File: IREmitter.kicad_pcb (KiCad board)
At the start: 2 copper layers, 36 parts, among them J1 JST Connector, J2 JST Connector, J3 Right Header, J4 Left Header, SW1 Switch, U1 MOSFET, U2 H-Bridge, U3 Voltage Regulator, U4 STM32F205RGTx

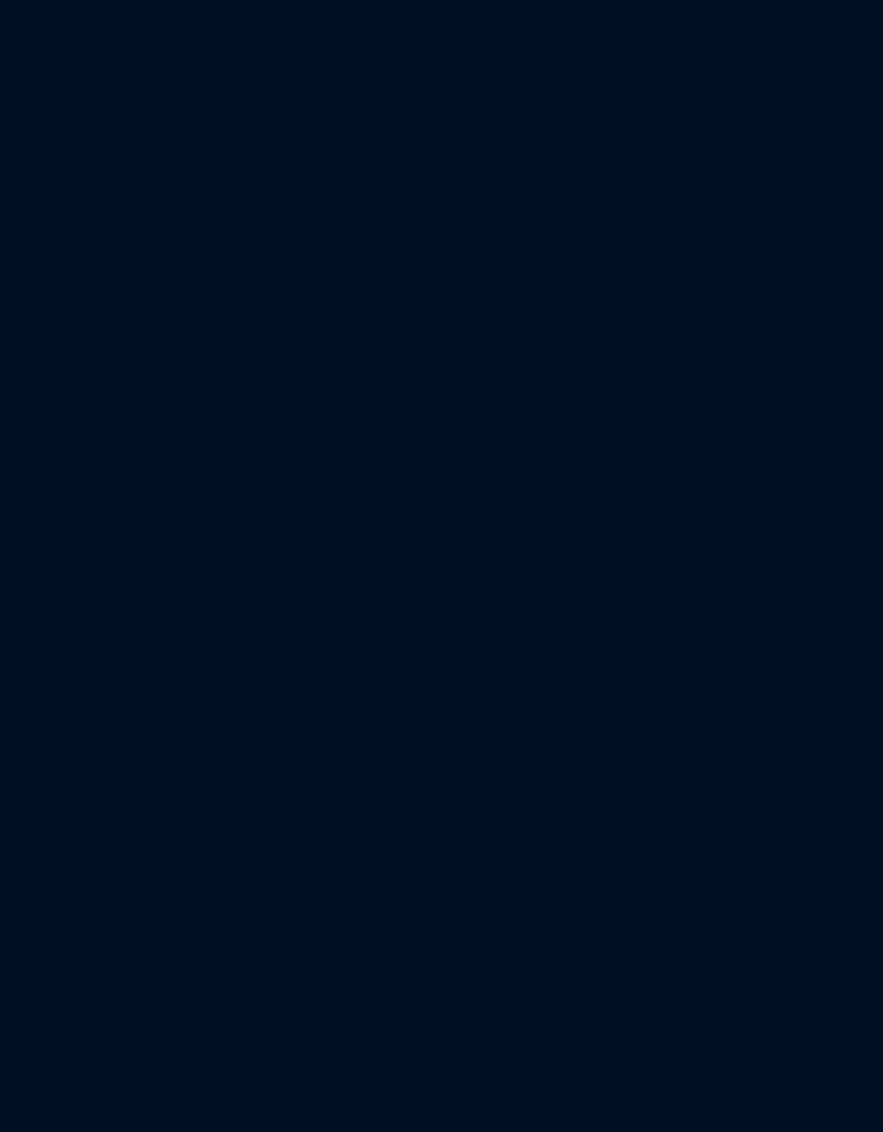
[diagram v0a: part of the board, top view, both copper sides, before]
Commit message: redid the 4 emitters receivers, fixed orientation of LEDS and going to continue adding footprints and replace the 60ohm resistors with 300ohm ones
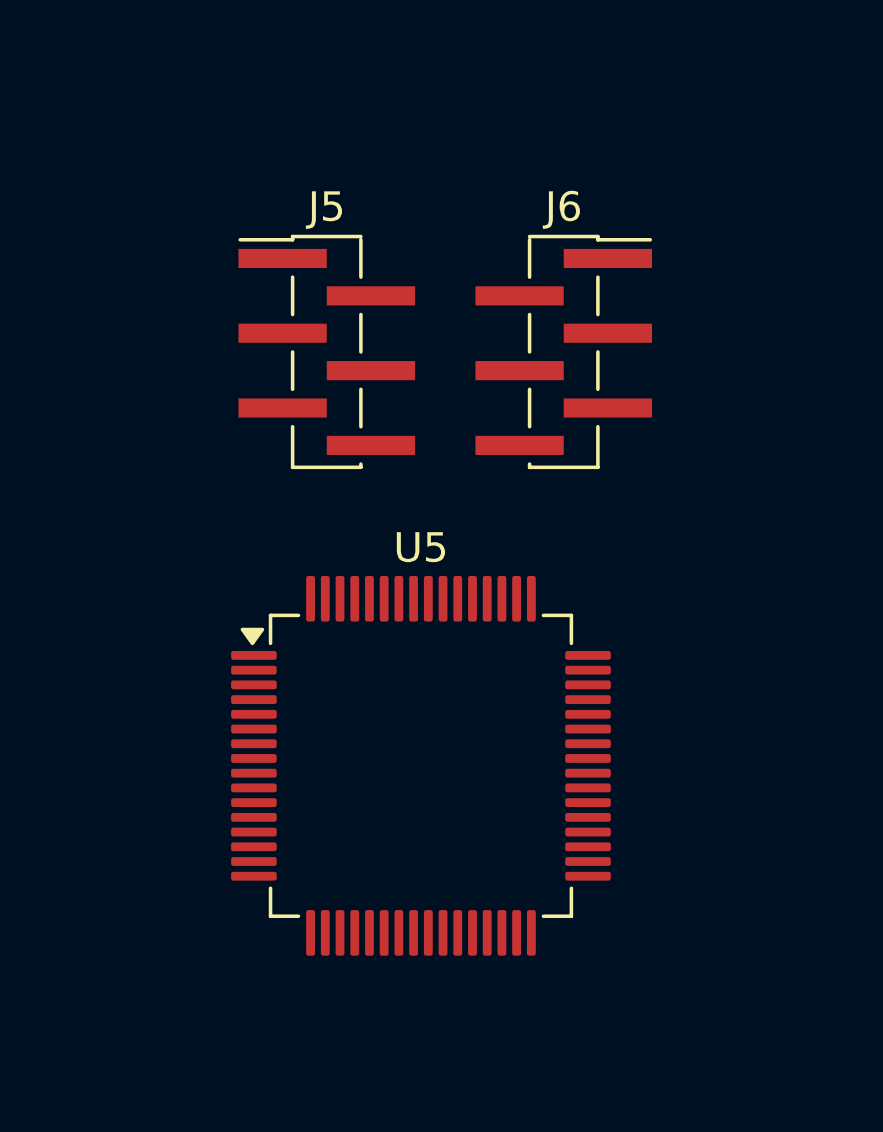
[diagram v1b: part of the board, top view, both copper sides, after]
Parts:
- added J5: Left Header, Connector_PinHeader_1.27mm:PinHeader_1x06_P1.27mm_Vertical_SMD_Pin1Left, F.Cu at (104.6, 45.2)
- added J6: Right Header, Connector_PinHeader_1.27mm:PinHeader_1x06_P1.27mm_Vertical_SMD_Pin1Right, F.Cu at (112.7, 45.2)
- added U5: STM32F205RGTx, Package_QFP:LQFP-64_10x10mm_P0.5mm, F.Cu at (107.8, 59.2)

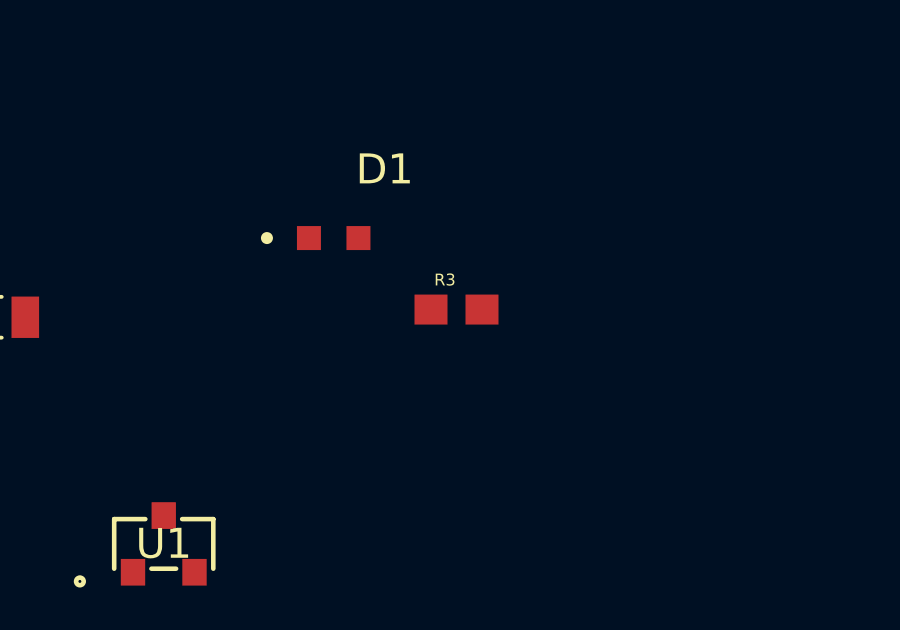
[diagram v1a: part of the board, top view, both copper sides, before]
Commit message: LED changes, mosfet footprint fixed
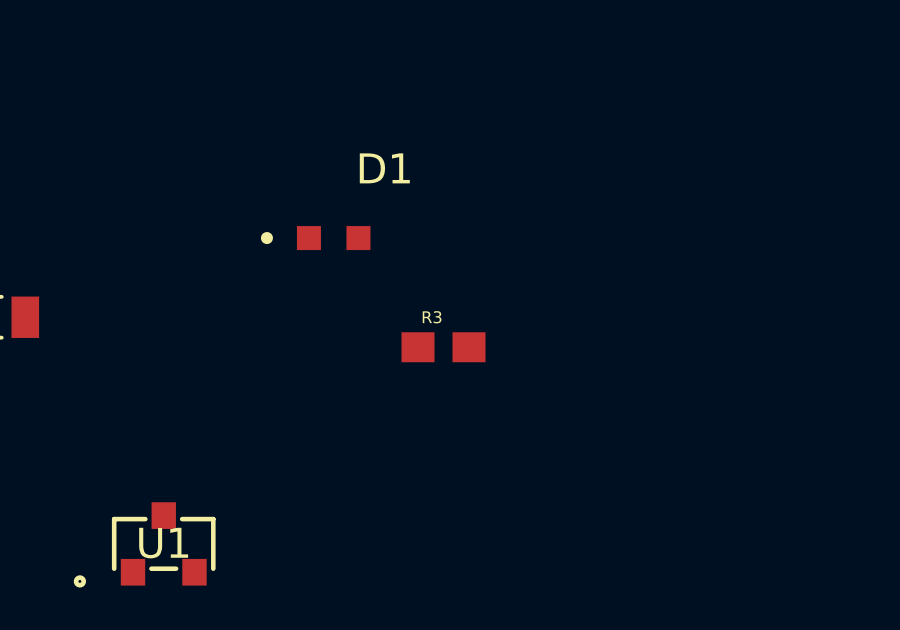
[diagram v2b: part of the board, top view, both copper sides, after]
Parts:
- moved R3 1.33 mm to (73.3, 109.0)
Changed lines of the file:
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@@
 	(footprint "RC0603FR_0747KL:RESC1608X55"
 		(layer "F.Cu")
-		(at 73.7834 107.7434)
+		(at 73.35 109)
 		(descr "<b>RESISTOR</b>")
 		(property "Reference" "R3"

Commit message: PCB tentative finished
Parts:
- removed A1: IR Receiver, ALS_PT19_315C_L177_TR8:XDCR_ALS-PT19-315C_L177_TR8
- removed C16: 0.1 µF, 0.1µFCapacitor_footprints:CAP_0402_N_WAL-L
- removed C17: 1 µF, CL10B105KP8NNNC:CAPC1608X90N
- removed C18: 10 µF, CL21B106KOQNNNE:CAPC2012X140N
- removed C19: 22 µF, CL21A226MPQNNNE:CAPC2012X140N
- removed J2: JST Connector, B2B_PH_K_S:JST_B2B-PH-K-S
- removed J3: Right Header, Connector_PinHeader_1.27mm:PinHeader_1x06_P1.27mm_Vertical_SMD_Pin1Right
- removed J4: Left Header, Connector_PinHeader_1.27mm:PinHeader_1x06_P1.27mm_Vertical_SMD_Pin1Left
- removed SW1: Switch, Switch_FSM4JSMATR_footprint:SW_4-1437565-2
- added C20: 2.2 µF, 2.2uF_CL21A226MPQNNNE:CAPC2012X140N, F.Cu at (131.4, 58.2)
- added C21: 2.2 µF, 2.2uF_CL21A226MPQNNNE:CAPC2012X140N, F.Cu at (132.2, 73.4)
- added C25: 10 µF, Ceramic_Capacitor_10uF_GRM21BC81C106KA73L:CAPC2012X140N, F.Cu at (149.7, 53.9)
- added C29: 1 µF, 1uF_CL10B105KP8NNNC:CAPC1608X90N, F.Cu at (151.2, 58.0)
- added C31: 4.7 µF, Ceramic_Capacitor_4.7uF_CL21A475KAQNNNE:CAPC2012X140N, F.Cu at (122.4, 53.8)
- added C33: 10 µF, Ceramic_Capacitor_10uF_GRM21BC81C106KA73L:CAPC2012X140N, F.Cu at (134.9, 98.2)
- added C35: 4.7 µF, Ceramic_Capacitor_4.7uF_CL21A475KAQNNNE:CAPC2012X140N, F.Cu at (131.3, 98.2)
- added C36: 4.7 µF, Ceramic_Capacitor_4.7uF_CL21A475KAQNNNE:CAPC2012X140N, F.Cu at (152.7, 81.8)
- added C37: 10 µF, Ceramic_Capacitor_10uF_GRM21BC81C106KA73L:CAPC2012X140N, F.Cu at (114.4, 107.6)
- added C38: 22 µF, Ceramic_Capacitor_22uF_CL21A226KPCLRNC:CAPC2012X95N, F.Cu at (101.6, 115.2)
- added D2: IR Emitter, IR_Emitter_TSAL6400:LEDRD254W55D595H900, F.Cu at (180.0, 57.8)
- added D3: IR Emitter, IR_Emitter_TSAL6400:LEDRD254W55D595H900, F.Cu at (161.8, 39.6)
- added D4: IR Emitter, IR_Emitter_TSAL6400:LEDRD254W55D595H900, F.Cu at (126.2, 39.6)
- added D5: Power Indicator LED, LED_WL-TMRC_5MM:WL-TMRC_5MM, F.Cu at (168.8, 76.5)
- added D6: User LED, LED_WL-TMRC_5MM:WL-TMRC_5MM, F.Cu at (115.6, 72.8)
- added D7: User LED, LED_WL-TMRC_5MM:WL-TMRC_5MM, F.Cu at (125.1, 72.8)
- added J7: JST Connector, JST_Connector_B2B-PH-K-S:JST_B2B-PH-K-S, F.Cu at (122.0, 105.2)
- added J8: JST Connector, JST_Connector_B2B-PH-K-S:JST_B2B-PH-K-S, F.Cu at (122.0, 112.1)
- added Motor1: ~, Pololu_Motor:Pololu_Motor, F.Cu at (183.2, 89.5)
- added Motor2: ~, Pololu_Motor:Pololu_Motor, F.Cu at (104.8, 86.5)
- added Q1: IR Receiver, IR_Receiver_ul_LTR-4206E:NoneP157X157-2_LTO, F.Cu at (108.0, 66.1)
- added Q2: IR Receiver, IR_Receiver_ul_LTR-4206E:NoneP157X157-2_LTO, F.Cu at (180.0, 66.1)
- added Q3: IR Receiver, IR_Receiver_ul_LTR-4206E:NoneP157X157-2_LTO, F.Cu at (167.5, 39.6)
- added Q4: IR Receiver, IR_Receiver_ul_LTR-4206E:NoneP157X157-2_LTO, F.Cu at (118.0, 39.6)
- added R10: 47 kOhm, 47_kohm_RC0603FR-0747KL:RESC1608X55, F.Cu at (120.3, 46.7)
- added R11: 51 Ohm, 51_ohm_RC0805FR-0751RL:RESC2012X60N, F.Cu at (131.1, 43.4)
- added R12: 10 kOhm, 10_kohm_RMCF0805FT10K0:RESC2012X65N, F.Cu at (143.5, 80.5)
- added R13: 10 kOhm, 10_kohm_RMCF0805FT10K0:RESC2012X65N, F.Cu at (136.0, 56.1)
- added R14: 100 Ohm, 100_ohm_CRCW0603100RFKEA:RESC1508X50N, F.Cu at (111.3, 50.7)
- added R15: 47 kOhm, 47_kohm_RC0603FR-0747KL:RESC1608X55, F.Cu at (118.2, 53.8)
- added R16: 51 Ohm, 51_ohm_RC0805FR-0751RL:RESC2012X60N, F.Cu at (115.0, 61.0)
- added R17: 1.8 kOhm, 1.8_kohm_RMCF0805JT1K80:RESC2012X65N, F.Cu at (108.0, 71.9)
- added R18: 330 Ohm, 330_ohm_RC0603FR-07330RL:RESC1607X60N, F.Cu at (175.3, 79.3)
- added R19: 1.8 kOhm, 1.8_kohm_RMCF0805JT1K80:RESC2012X65N, F.Cu at (180.0, 71.9)
- added R20: 1.8 kOhm, 1.8_kohm_RMCF0805JT1K80:RESC2012X65N, F.Cu at (173.3, 45.6)
- added R21: 1.8 kOhm, 1.8_kohm_RMCF0805JT1K80:RESC2012X65N, F.Cu at (113.8, 42.9)
- added R6: 100 Ohm, 100_ohm_CRCW0603100RFKEA:RESC1508X50N, F.Cu at (157.6, 54.5)
- added R8: 51 Ohm, 51_ohm_RC0805FR-0751RL:RESC2012X60N, F.Cu at (166.7, 45.9)
- added R9: 100 Ohm, 100_ohm_CRCW0603100RFKEA:RESC1508X50N, F.Cu at (133.2, 47.6)
- added S1: EG1218, Slide_Switch_EG1218:SW_EG1218, F.Cu at (128.1, 108.5)
- added SW2: Switch, Switch_4-1437565-2:SW_4-1437565-2, F.Cu at (169.5, 110.2)
- added U7: H-Bridge, H-Bridge_L293DD:SOIC127P1032X265-20N, F.Cu at (143.8, 93.4)
- added U8: Voltage Regulator, Voltage_Regulator_AZ1117IH-3.3TRG1:SOT230P700X185-4N, F.Cu at (111.3, 115.2)
- C1, C4, C6: value 4.7 µF -> 0.1 µF; footprint CL10A475KP8NNNC:CAPC1608X90N -> Ceramic_Capacitor_0.1uF_CL21B104KBCNNNC:CAPC2012X95N
- C10: value 2.2 µF -> 4.7 µF; footprint CL10B225KP8NNNC:CAPC1608X90N -> Ceramic_Capacitor_4.7uF_CL21A475KAQNNNE:CAPC2012X140N
- C11: value 0.1 uF -> 0.1 µF; footprint 0.1µFCapacitor_footprints:CAP_0402_N_WAL-L -> Ceramic_Capacitor_0.1uF_CL21B104KBCNNNC:CAPC2012X95N
- C12, C14: value 0.1 µF -> 4.7 µF; footprint 0.1µFCapacitor_footprints:CAP_0402_N_WAL-L -> Ceramic_Capacitor_4.7uF_CL21A475KAQNNNE:CAPC2012X140N
- C13, C2, C5, C7, C8: footprint 0.1µFCapacitor_footprints:CAP_0402_N_WAL-L -> Ceramic_Capacitor_0.1uF_CL21B104KBCNNNC:CAPC2012X95N
- C15, C3: value 10 µF -> 0.1 µF; footprint CL21B106KOQNNNE:CAPC2012X140N -> Ceramic_Capacitor_0.1uF_CL21B104KBCNNNC:CAPC2012X95N
- C9: value 2.2 µF -> 0.1 µF; footprint CL10B225KP8NNNC:CAPC1608X90N -> Ceramic_Capacitor_0.1uF_CL21B104KBCNNNC:CAPC2012X95N
- D1: footprint APT1608F3C:LED_APT1608F3C -> IR_Emitter_TSAL6400:LEDRD254W55D595H900
- J1: value JST Connector -> PPTC041LFBN-RC; footprint B2B_PH_K_S:JST_B2B-PH-K-S -> Connector_01x04_PPTC041LFBN-RC:SULLINS_PPTC041LFBN-RC
- R1: value 51 Ohm -> 330 Ohm; footprint RC0805FR_0751RL:RESC2012X60N -> 330_ohm_RC0603FR-07330RL:RESC1607X60N
- R2: value 100 Ohm -> 330 Ohm; footprint CRCW0603100RFKEA:RESC1508X50N -> 330_ohm_RC0603FR-07330RL:RESC1607X60N
- R3: value 47 kOhm -> 100 Ohm; footprint RC0603FR_0747KL:RESC1608X55 -> 100_ohm_CRCW0603100RFKEA:RESC1508X50N
- R4: value RMCF0805JT1K80 -> 47 kOhm; footprint RMCF0805JT1K80:RESC2012X65N -> 47_kohm_RC0603FR-0747KL:RESC1608X55
- R5: value 10 kOhm -> 51 Ohm; footprint RMCF0805FT10K0:RESC2012X65N -> 51_ohm_RC0805FR-0751RL:RESC2012X60N
- R7: value 10 kOhm -> 47 kOhm; footprint RMCF0805FT10K0:RESC2012X65N -> 47_kohm_RC0603FR-0747KL:RESC1608X55
- U1: footprint MOSFET_footprints:SOT-23_1_DIO -> MOSFET_ul_2N7002-7-F:SOT-23_1_DIO
- U2: value H-Bridge -> MOSFET; footprint hbridge_L293DD:SOIC127P1032X265-20N -> MOSFET_ul_2N7002-7-F:SOT-23_1_DIO
- U3: value Voltage Regulator -> MOSFET; footprint AZ1117IH-3.3TRG1:SOT230P700X185-4N -> MOSFET_ul_2N7002-7-F:SOT-23_1_DIO
- U4: value STM32F205RGTx -> MOSFET; footprint Package_QFP:LQFP-64_10x10mm_P0.5mm -> MOSFET_ul_2N7002-7-F:SOT-23_1_DIO
- moved C2 112.4 mm to (154.6, 70.4), turned to 180 degrees
- moved C15 110.0 mm to (136.1, 41.8), turned to 180 degrees
- moved C1 108.2 mm to (151.3, 60.5)
- moved R3 106.4 mm to (168.6, 61.6)
- moved C13 102.3 mm to (170.8, 52.3), turned to 180 degrees
- moved C14 101.8 mm to (136.2, 38.1)
- moved U2 96.1 mm to (173.6, 57.5)
- moved C10 96.1 mm to (174.3, 69.1), turned to -90 degrees
- moved C12 96.0 mm to (162.3, 52.2), turned to 180 degrees
- moved U4 88.8 mm to (126.8, 46.6), turned to 90 degrees
- moved C6 87.5 mm to (151.4, 74.9), turned to 180 degrees
- moved C5 83.1 mm to (136.1, 76.2), turned to 90 degrees
- moved R7 82.9 mm to (151.7, 47.7)
- moved U1 78.2 mm to (114.3, 55.6), turned to 180 degrees
- moved C8 77.1 mm to (127.1, 53.8), turned to -90 degrees
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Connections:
- C10 pad 1: GND -> 3V3
- C10 pad 2: Net-(U4-VCAP_2) -> GND
- C11 pad 1: NRST -> GND
- C11 pad 2: GND -> 3V3
- C12 pad 1: GND -> 3V3
- C12 pad 2: 3V3 -> GND
- C14 pad 1: GND -> 3V3
- C14 pad 2: 3V3 -> GND
- C3 pad 1: VCC -> GND
- C3 pad 2: MGND -> 3V3
- C4 pad 1: MGND -> GND
- C4 pad 2: VCC -> 3V3
- C5 pad 2: VCC -> 3V3
- C6 pad 1: VCC -> GND
- C6 pad 2: GND -> 3V3
- C7 pad 1: GND -> /MM-MCU/NRST
- C7 pad 2: 3V3 -> GND
- C9 pad 2: Net-(U4-VCAP_1) -> VCC
- J1 pad 1: VCC -> /MM-MCU/NRST
- J1 pad 2: Net-(J1-Pad2) -> /MM-MCU/SWDIO
- R1 pad 1: Net-(D1-Pad2) -> GND
- R1 pad 2: 3V3 -> Net-(D7-Pad2)
- R2 pad 1: PC9 (to be assigned) -> GND
- R2 pad 2: Net-(U1-G) -> Net-(D6-Pad2)
- R3 pad 1: GND -> /MM-IR-Emitter/IR_EMITTER_2
- R3 pad 2: Net-(U1-G) -> Net-(U2-G)
- R4 pad 2: PC5 (to be assigned) -> Net-(U2-G)
- R5 pad 1: GND -> Net-(D2-PadA)
- R5 pad 2: Net-(U4-BOOT0) -> 3V3
- R7 pad 1: Net-(U4-PB2) -> GND
- R7 pad 2: GND -> Net-(U3-G)
- U2 pad 1: 3V3 -> Net-(U2-G)
- U2 pad 2: PB6 -> GND
- U2 pad 3: ML2 -> Net-(U2-D)
- U3 pad 1: GND -> Net-(U3-G)
- U3 pad 2: 3V3 -> GND
- U3 pad 3: VCC -> Net-(U3-D)
- U4 pad 1: 3V3 -> Net-(U4-G)
- U4 pad 2: unconnected-(U4-PC13-Pad2) -> GND
- U4 pad 3: unconnected-(U4-PC14-Pad3) -> Net-(U4-D)
- U5 pad 10: unconnected-(U5-PC2-Pad10) -> /MM-IR-Emitter/IR_EMITTER_3
- U5 pad 11: unconnected-(U5-PC3-Pad11) -> /MM-IR-Receiver/IR_RECEIVER_3
- U5 pad 22: /MM-IR-Receiver/PA6 -> /MM-IR-Emitter/IR_EMITTER_4
- U5 pad 23: /MM-IR-Emitter/PA7 -> /MM-IR-Receiver/IR_RECEIVER_4
- U5 pad 24: Net-(U5-PC4) -> /MM-IR-Emitter/IR_EMITTER_1
- U5 pad 25: Net-(U5-PC5) -> /MM-IR-Receiver/IR_RECEIVER_1
- U5 pad 37: unconnected-(U5-PC6-Pad37) -> Net-(U5-PC6)
- U5 pad 38: unconnected-(U5-PC7-Pad38) -> Net-(U5-PC7)
- U5 pad 46: SWDIO -> /MM-MCU/SWDIO
- U5 pad 49: SWCLK -> /MM-MCU/SWCLK
- U5 pad 58: /MM-MCU/INPUT_1 -> /MM-MCU/INPUT_2
- U5 pad 59: /MM-MCU/INPUT_2 -> /MM-MCU/INPUT_1
- U5 pad 8: unconnected-(U5-PC0-Pad8) -> /MM-IR-Emitter/IR_EMITTER_2
- U5 pad 9: unconnected-(U5-PC1-Pad9) -> /MM-IR-Receiver/IR_RECEIVER_2
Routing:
- net 3V3: track 0.00 -> 385.6 mm, vias 0 -> 2
- net /MM-MCU/NRST: track 0.00 -> 72.4 mm, vias 0 -> 1
- net VCC: track 0.00 -> 67.3 mm
- net /MM-IR-Receiver/IR_RECEIVER_1: track 0.00 -> 52.3 mm, vias 0 -> 2
- net /MM-MCU/SWDIO: track 0.00 -> 50.7 mm, vias 0 -> 1
- net /MM-MCU/SWCLK: track 0.00 -> 46.6 mm, vias 0 -> 1
- net /MM-IR-Receiver/IR_RECEIVER_4: track 0.00 -> 44.5 mm
- net /MM-IR-Receiver/IR_RECEIVER_3: track 0.00 -> 43.0 mm, vias 0 -> 4
- net /MM-IR-Receiver/IR_RECEIVER_2: track 0.00 -> 40.4 mm, vias 0 -> 2
- net /MM-MCU/INPUT_4: track 0.00 -> 38.9 mm
- net /MM-IR-Emitter/IR_EMITTER_1: track 0.00 -> 38.0 mm, vias 0 -> 2
- net /MM-MCU/INPUT_3: track 0.00 -> 30.5 mm
- net MR1: track 0.00 -> 29.9 mm, vias 0 -> 2
- net /MM-MCU/INPUT_2: track 0.00 -> 29.9 mm, vias 0 -> 4
- net Net-(U5-PC6): track 0.00 -> 26.7 mm
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- added copper zone on B.Cu, net GND
- added copper zone on F.Cu, net GND
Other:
- board outline added: 94 x 92.6 mm

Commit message: finished edits on PCB - hopefully final
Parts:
- removed J5: Left Header, Connector_PinHeader_1.27mm:PinHeader_1x06_P1.27mm_Vertical_SMD_Pin1Left
- removed J6: Right Header, Connector_PinHeader_1.27mm:PinHeader_1x06_P1.27mm_Vertical_SMD_Pin1Right
- added J2: Conn_01x06, Connector_PinHeader_2.54mm:PinHeader_1x06_P2.54mm_Vertical, F.Cu at (139.0, 103.6)
- added J3: Conn_01x06, Connector_PinHeader_2.54mm:PinHeader_1x06_P2.54mm_Vertical, F.Cu at (148.7, 103.6)
- moved J7 0.80 mm to (122.0, 104.4)
- moved J8 0.80 mm to (122.0, 111.3)
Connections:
- J8 pad 2: GND -> MGND
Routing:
- net MGND: track 25.7 -> 57.0 mm
- net 3V3: track 385.6 -> 369.0 mm
- net MR1: track 29.9 -> 17.5 mm
- net MR2: track 18.7 -> 12.6 mm
- net ML1: track 16.6 -> 13.9 mm, vias 4 -> 2
- net ML2: track 23.5 -> 22.1 mm
- net GND: vias 37 -> 38
